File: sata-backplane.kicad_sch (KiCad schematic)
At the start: 42 parts, among them J5 457180002, J6 G40H3132212HR

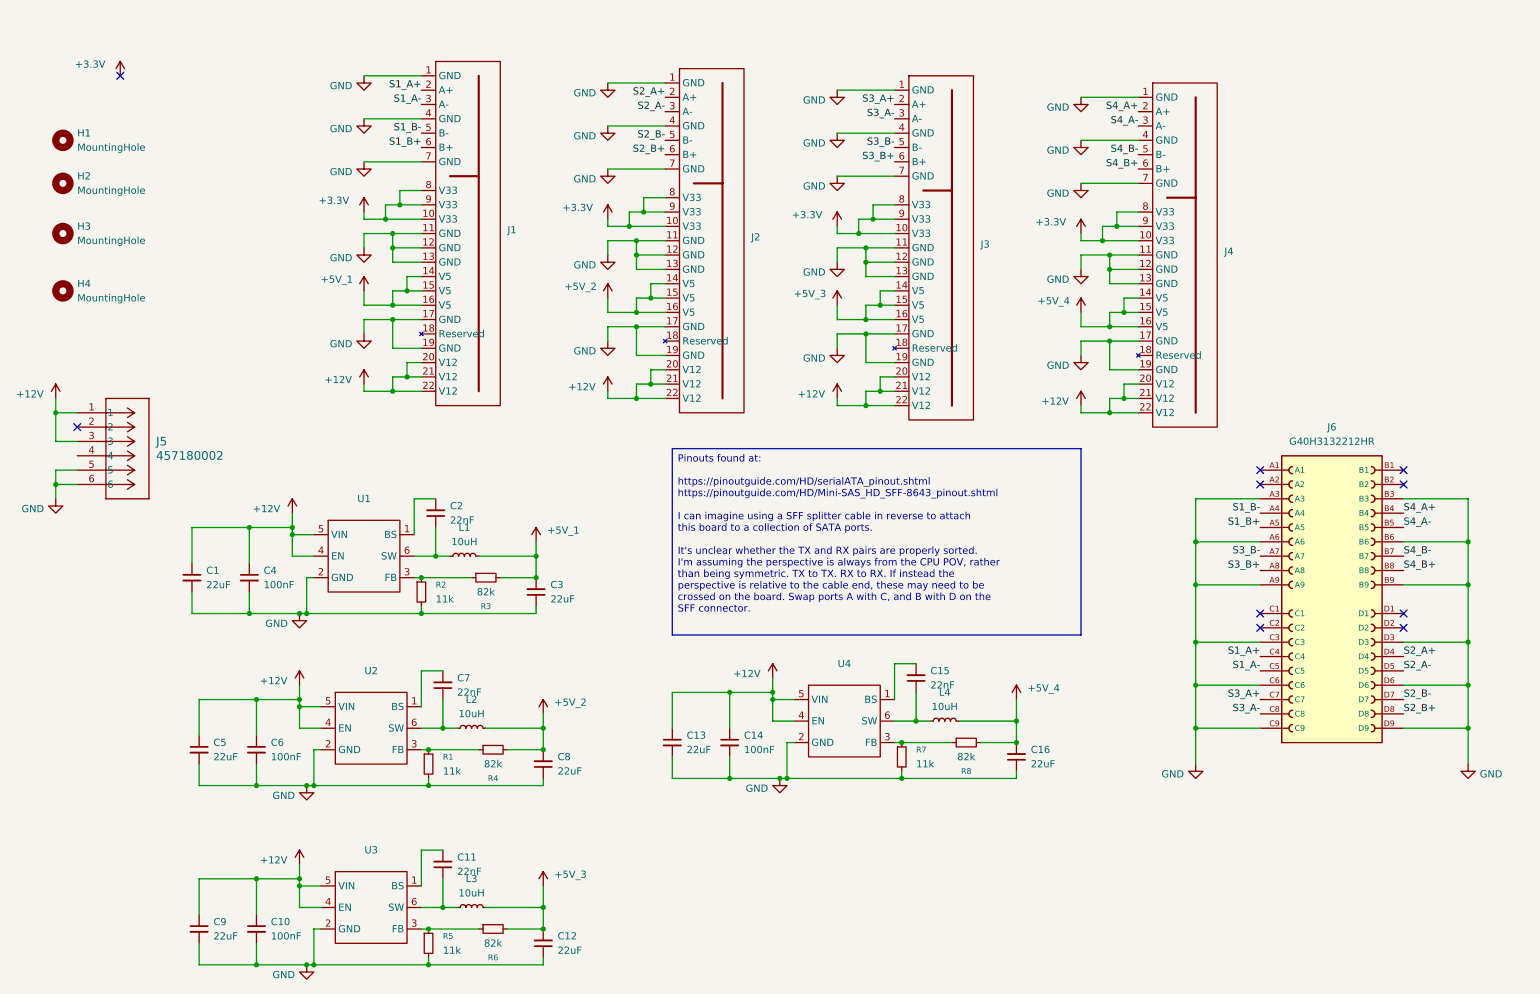
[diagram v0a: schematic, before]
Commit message: Switch to two 3A converters from 4 2A
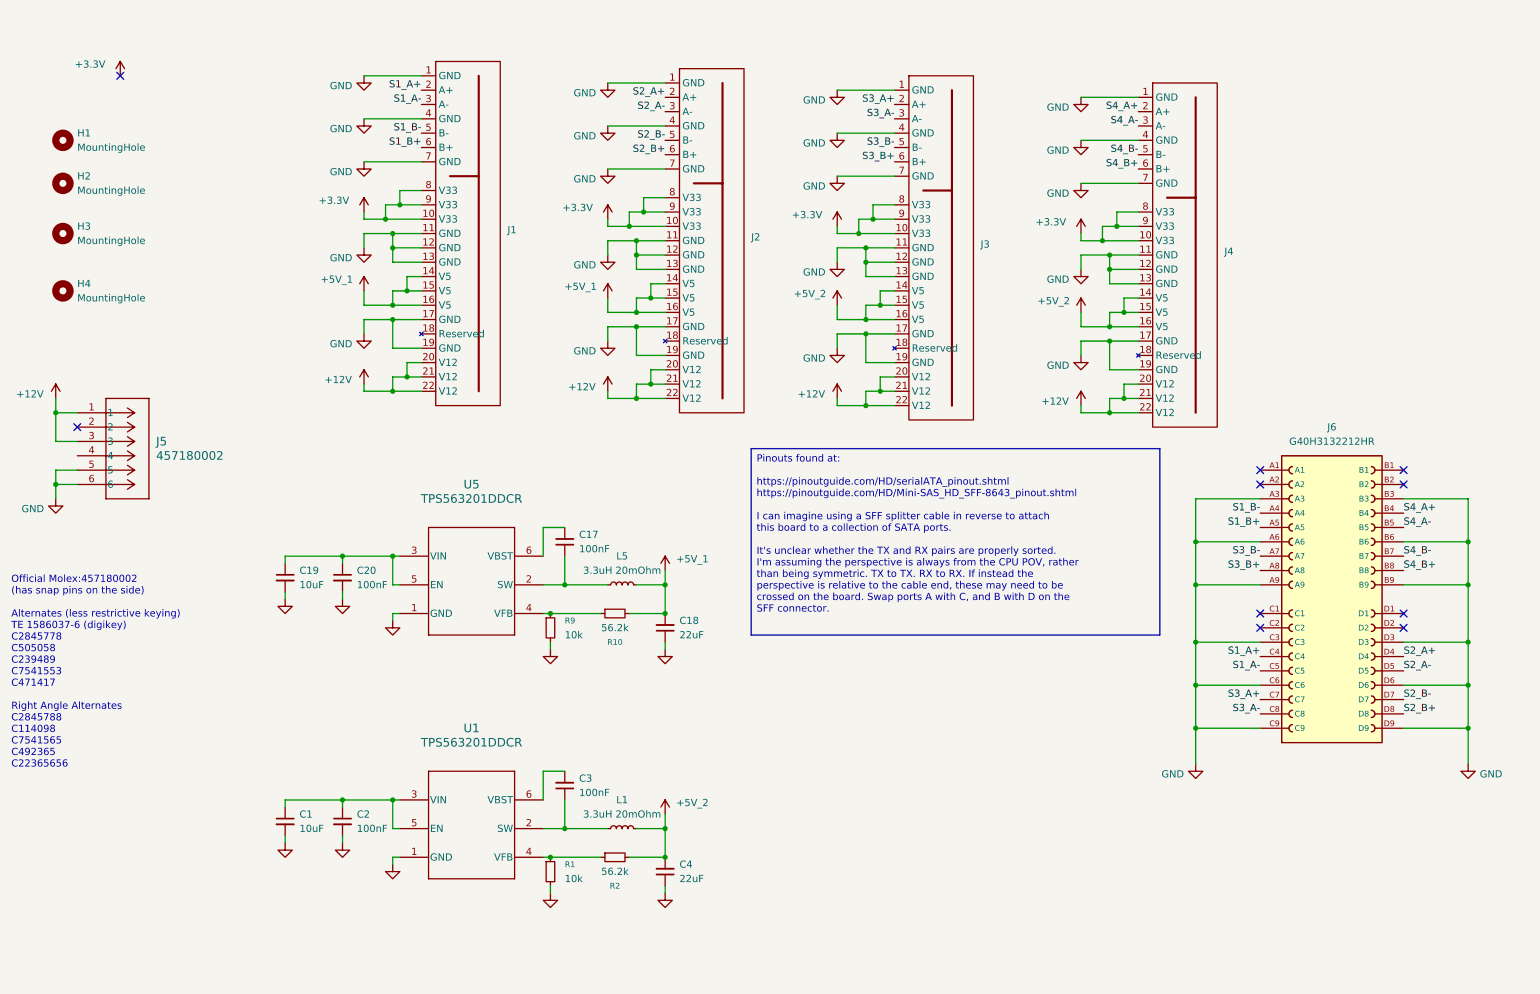
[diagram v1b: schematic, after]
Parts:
- removed C10, C14, C6: 100nF, Capacitor_SMD:C_0603_1608Metric_Pad1.08x0.95mm_HandSolder, symbol Device:C_Small
- removed C11, C15, C7: 22nF, Capacitor_SMD:C_0603_1608Metric_Pad1.08x0.95mm_HandSolder, symbol Device:C_Small
- removed C12, C13, C16, C5, C8, C9: 22uF, Capacitor_SMD:C_0603_1608Metric_Pad1.08x0.95mm_HandSolder, symbol Device:C_Small
- removed L2, L3, L4: 10uH, 00-Local:SL0420, symbol Device:L_Small
- removed R3, R4, R6, R8: 82k, Resistor_SMD:R_0603_1608Metric_Pad0.98x0.95mm_HandSolder, symbol Device:R_Small
- removed R5, R7: 11k, Resistor_SMD:R_0603_1608Metric_Pad0.98x0.95mm_HandSolder, symbol Device:R_Small
- removed U1, U2, U3, U4: ~, Package_TO_SOT_SMD:SOT-23-6, symbol 00_Local:MT2492
- added C17, C20: 100nF, Capacitor_SMD:C_0603_1608Metric_Pad1.08x0.95mm_HandSolder, symbol Device:C_Small
- added C18: 22uF, Capacitor_SMD:C_0603_1608Metric_Pad1.08x0.95mm_HandSolder, symbol Device:C_Small
- added C19: 10uF, Capacitor_SMD:C_0603_1608Metric_Pad1.08x0.95mm_HandSolder, symbol Device:C_Small
- added L5: 3.3uH 20mOhm, 00-Local:SL0420, symbol Device:L_Small
- added R10: 56.2k, Resistor_SMD:R_0603_1608Metric_Pad0.98x0.95mm_HandSolder, symbol Device:R_Small
- added R9: 10k, Resistor_SMD:R_0603_1608Metric_Pad0.98x0.95mm_HandSolder, symbol Device:R_Small
- added U1, U5: TPS563201DDCR, Package_TO_SOT_SMD:SOT-23-6_Handsoldering, symbol 00_Local:TPS563201DDCR
- C1: value 22uF -> 10uF
- C2: value 22nF -> 100nF
- C3: value 22uF -> 100nF
- C4: value 100nF -> 22uF
- J5: footprint 00-Local:CONN_SD-45718-001_MOL -> 00_Local:CONN_SD-45718-001_MOL; symbol 2025-05-24_19-30-13:457180002 -> 00_Local:457180002
- J6: footprint G40H3132212HR:AMPHENOL_G40H3132212HR -> 00-Local:AMPHENOL_G40H3132212HR; symbol G40H3132212HR:G40H3132212HR -> 00_Local:G40H3132212HR
- L1: value 10uH -> 3.3uH 20mOhm; LCSC (none) -> C22463807
- R1: value 11k -> 10k
- R2: value 11k -> 56.2k
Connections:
- net +5V_3 is gone; now on net +5V_2: J3.14 (V5), J3.15 (V5), J3.16 (V5)
- net +5V_4 is gone; now on net +5V_2: J4.14 (V5), J4.15 (V5), J4.16 (V5)
- net +12V: no longer C1.1, C4.1
- net +5V_1: now also J2.14 (V5), J2.15 (V5), J2.16 (V5), C18.2, L5.2, R10.2; no longer C3.2, L1.2
- net +5V_2: now also C4.2, L1.2, R2.2; no longer J2.14 (V5), J2.15 (V5), J2.16 (V5)
- net GND: now also C2.2, C4.1, C18.1, C19.2, C20.2, R9.2, U1.1 (GND), U5.1 (GND); no longer C3.1, C4.2, R2.2
- net at R2.1: now also R1.1, U1.4 (VFB)
- net at L1.1: now also C3.1, U1.2 (SW); no longer C2.1
- new net: C17.1, L5.1, U5.2 (SW)
- new net: C17.2, U5.6 (VBST)
- new net: C3.2, U1.6 (VBST)
- new net: C1.1, C2.1, U1.3 (VIN), U1.5 (EN)
- new net: R10.1, R9.1, U5.4 (VFB)
- new net: C19.1, C20.1, U5.3 (VIN), U5.5 (EN)
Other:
- note added: "Official Molex:457180002 (has snap pins on the side) Alternates (less restrictive keying) TE 1586037-6 (digikey) C2845778 C505058 C239489 C7541553 C471417 Right Angle Alternates C2845788 C114098 C7541565 C492365 C22365656"

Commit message: Rough layout
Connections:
- net +12V: now also C1.1, C19.1, C2.1, C20.1, U1.3 (VIN), U1.5 (EN), U5.3 (VIN), U5.5 (EN)
- net GND: now also J5.4
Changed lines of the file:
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@@
 	)
 	(junction
+		(at 68.58 161.29)
+		(diameter 0)
+		(color 0 0 0 0)
+	)
+	(junction
 		(at 271.78 115.57)
 		(diameter 0)
@@
 	)
 	(junction
+		(at 68.58 118.11)
+		(diameter 0)
+		(color 0 0 0 0)
+	)
+	(junction
 		(at 81.28 88.9)
 		(diameter 0)
@@
 	)
 	(junction
+		(at 21.59 102.87)
+		(diameter 0)
+		(color 0 0 0 0)
+	)
+	(junction
 		(at 83.82 71.12)
 		(diameter 0)
@@
 	(wire
 		(pts
+			(xy 25.4 100.33) (xy 21.59 100.33)
+		)
+		(stroke
+			(width 0)
+			(type default)
+		)
+	)
+	(wire
+		(pts
 			(xy 81.28 60.96) (xy 76.2 60.96)
 		)
@@
 	(wire
 		(pts
+			(xy 68.58 161.29) (xy 72.39 161.29)
+		)
+		(stroke
+			(width 0)
+			(type default)
+		)
+	)
+	(wire
+		(pts
 			(xy 223.52 140.97) (xy 234.95 140.97)
 		)
@@
 	(wire
 		(pts
+			(xy 21.59 100.33) (xy 21.59 102.87)
+		)
+		(stroke
+			(width 0)
+			(type default)
+		)
+	)
+	(wire
+		(pts
 			(xy 86.36 66.04) (xy 81.28 66.04)
 		)
@@
 	(wire
 		(pts
+			(xy 68.58 158.75) (xy 68.58 161.29)
+		)
+		(stroke
+			(width 0)
+			(type default)
+		)
+	)
+	(wire
+		(pts
 			(xy 160.02 76.2) (xy 165.1 76.2)
 		)
@@
 	(wire
 		(pts
+			(xy 68.58 115.57) (xy 68.58 118.11)
+		)
+		(stroke
+			(width 0)
+			(type default)
+		)
+	)
+	(wire
+		(pts
 			(xy 21.59 92.71) (xy 25.4 92.71)
 		)
@@
 	(wire
 		(pts
-			(xy 62.23 118.11) (xy 72.39 118.11)
+			(xy 62.23 118.11) (xy 68.58 118.11)
 		)
 		(stroke
@@
 	(wire
 		(pts
+			(xy 68.58 118.11) (xy 72.39 118.11)
+		)
+		(stroke
+			(width 0)
+			(type default)
+		)
+	)
+	(wire
+		(pts
 			(xy 170.18 91.44) (xy 165.1 91.44)
 		)
@@
 	(wire
 		(pts
-			(xy 62.23 161.29) (xy 72.39 161.29)
+			(xy 62.23 161.29) (xy 68.58 161.29)
 		)
 		(stroke
@@
 	)
 	(symbol
+		(lib_id "power:+12V")
+		(at 68.58 158.75 0)
+		(unit 1)
+		(exclude_from_sim no)
+		(in_bom yes)
+		(on_board yes)
+		(dnp no)
+		(property "Reference" "#PWR039"
+			(at 68.58 162.56 0)
+			(effects
+				(font
+					(size 1.27 1.27)
+				)
+				(hide yes)
+			)
+		)
+		(property "Value" "+12V"
+			(at 64.008 157.988 0)
+			(effects
+				(font
+					(size 1.27 1.27)
+				)
+			)
+		)
+		(property "Footprint" ""
+			(at 68.58 158.75 0)
+			(effects
+				(font
+					(size 1.27 1.27)
+				)
+				(hide yes)
+			)
+		)
+		(property "Datasheet" ""
+			(at 68.58 158.75 0)
+			(effects
+				(font
+					(size 1.27 1.27)
+				)
+				(hide yes)
+			)
+		)
+		(property "Description" "Power symbol creates a global label with name \"+12V\""
+			(at 68.58 158.75 0)
+			(effects
+				(font
+					(size 1.27 1.27)
+				)
+				(hide yes)
+			)
+		)
+		(pin "1"
+		)
+		(instances
+			(project "sata-backplane"
+				(path "/09586197-2cbc-428a-b2c0-9ce846ccfbe7"
+					(reference "#PWR039")
+					(unit 1)
+				)
+			)
+		)
+	)
+	(symbol
 		(lib_id "power:GND")
 		(at 76.2 40.64 0)
@@
 					(unit 1)
 				)
+			)
+		)
+	)
+	(symbol
+		(lib_id "power:+12V")
+		(at 68.58 115.57 0)
+		(unit 1)
+		(exclude_from_sim no)
+		(in_bom yes)
+		(on_board yes)
+		(dnp no)
+		(property "Reference" "#PWR037"
+			(at 68.58 119.38 0)
+			(effects
+				(font
+					(size 1.27 1.27)
+				)
+				(hide yes)
+			)
+		)
+		(property "Value" "+12V"
+			(at 64.008 114.808 0)
+			(effects
+				(font
+					(size 1.27 1.27)
+				)
+			)
+		)
+		(property "Footprint" ""
+			(at 68.58 115.57 0)
+			(effects
+				(font
+					(size 1.27 1.27)
+				)
+				(hide yes)
+			)
+		)
+		(property "Datasheet" ""
+			(at 68.58 115.57 0)
+			(effects
+				(font
+					(size 1.27 1.27)
+				)
+				(hide yes)
+			)
+		)
+		(property "Description" "Power symbol creates a global label with name \"+12V\""
+			(at 68.58 115.57 0)
+			(effects
+				(font
+					(size 1.27 1.27)
+				)
+				(hide yes)
+			)
+		)
+		(pin "1"
+		)
+		(instances
+			(project "sata-backplane"
+				(path "/09586197-2cbc-428a-b2c0-9ce846ccfbe7"
+					(reference "#PWR037")
+					(unit 1)
+				)

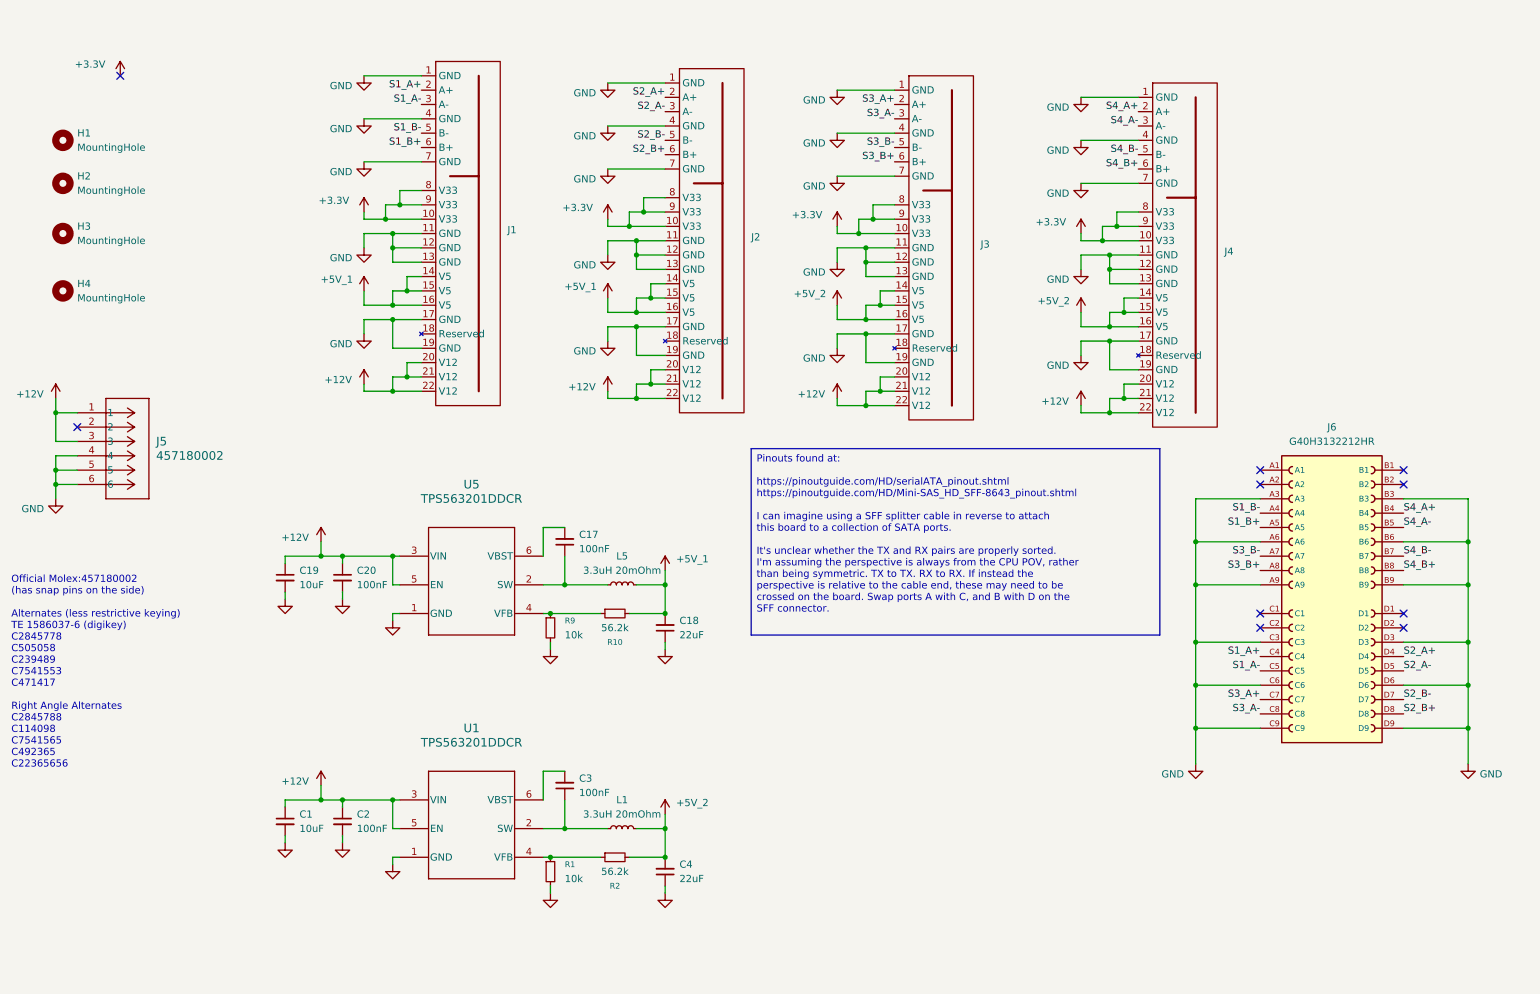
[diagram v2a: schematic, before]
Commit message: Wire up power
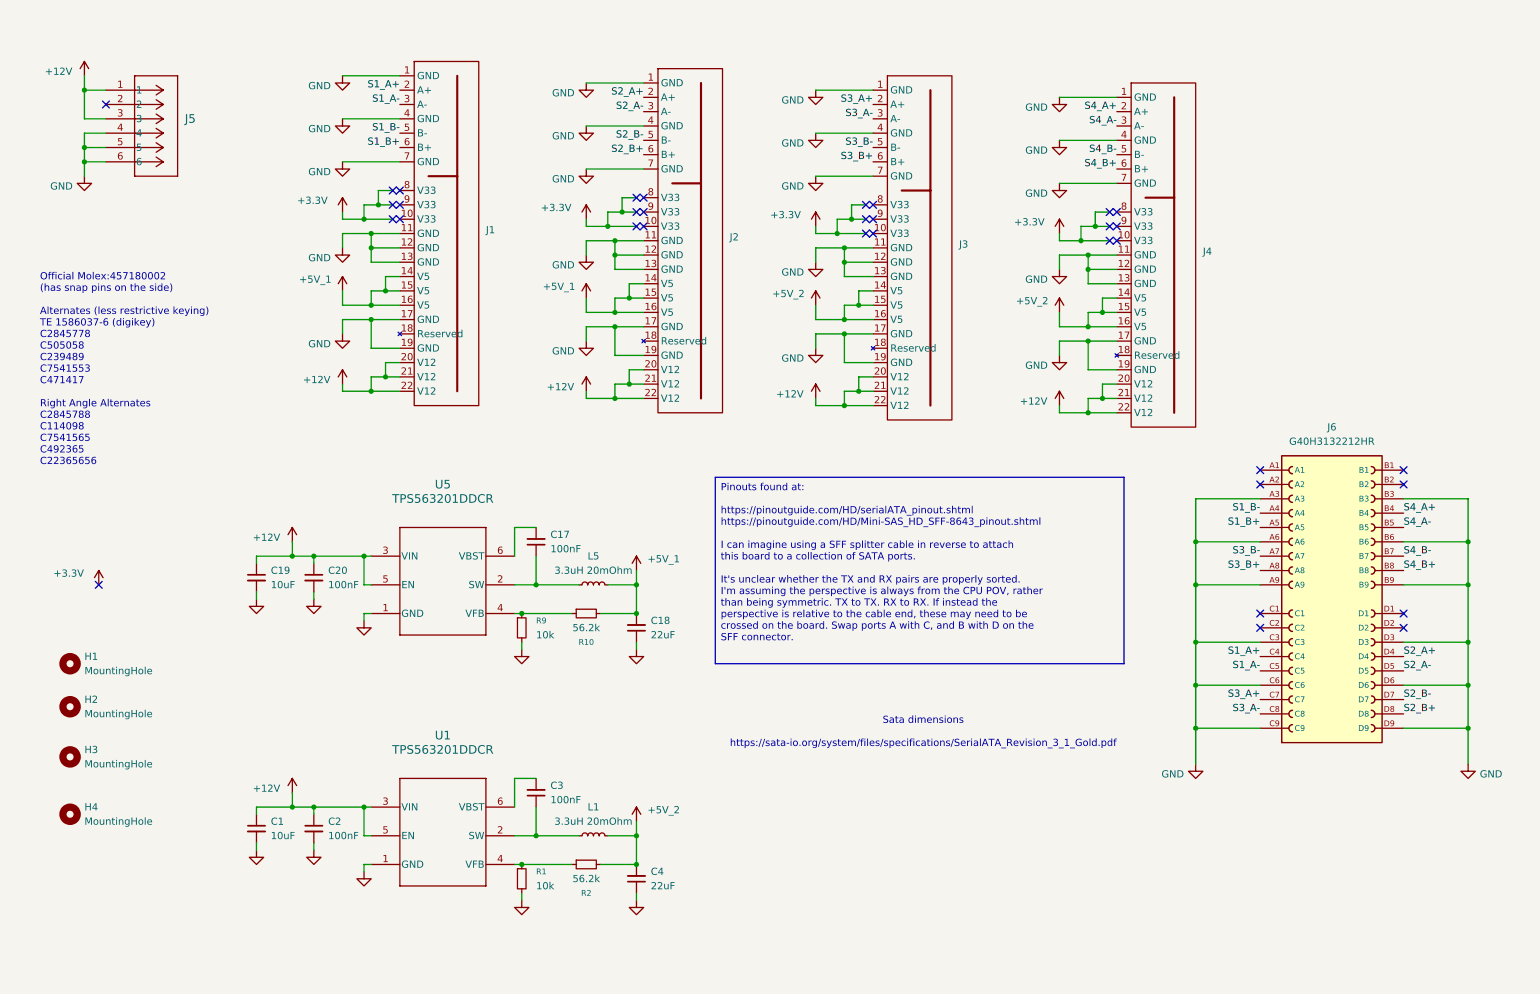
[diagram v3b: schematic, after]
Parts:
- U5: LCSC (none) -> C116592
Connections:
- net +3.3V: no longer J1.10 (V33), J1.8 (V33), J1.9 (V33), J2.10 (V33), J2.8 (V33), J2.9 (V33), J3.10 (V33), J3.8 (V33), J3.9 (V33), J4.10 (V33), J4.8 (V33), J4.9 (V33)
- no-connect marks 10 -> 34
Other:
- note added: "Sata dimensions https://sata-io.org/system/files/specifications/SerialATA_Revision_3_1_Gold.pdf"
- moved on the sheet: C1, C17, C18, C19, C2, C20, C3, C4, H1, H2, H3, H4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
